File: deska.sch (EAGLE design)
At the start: 15 parts, among them T1 TIP122, T2 TIP122, T3 TIP122, X2 NAPAJENI

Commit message: deska
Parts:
- removed X2: NAPAJENI, con-wago-508:W237-05P
- added LISTA: (no value), con-wago-500:W237-6
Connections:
- net +12V: now also LISTA-4.KL, LISTA-5.KL; no longer X2-4.KL
- net GND: now also LISTA-6.KL; no longer X2-1.KL
- net N$1: now also LISTA-3.KL; no longer X2-5.KL
- net N$2: now also LISTA-2.KL; no longer X2-3.KL
- net N$3: now also LISTA-1.KL; no longer X2-2.KL
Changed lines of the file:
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@@
 <grid distance="0.1" unitdist="inch" unit="inch" style="lines" multiple="1" display="no" altdistance="0.01" altunitdist="inch" altunit="inch"/>
 <layers>
-<layer number="1" name="Top" color="4" fill="1" visible="no" active="no"/>
-<layer number="16" name="Bottom" color="1" fill="1" visible="no" active="no"/>
-<layer number="17" name="Pads" color="2" fill="1" visible="no" active="no"/>
-<layer number="18" name="Vias" color="2" fill="1" visible="no" active="no"/>
-<layer number="19" name="Unrouted" color="6" fill="1" visible="no" active="no"/>
-<layer number="20" name="Dimension" color="15" fill="1" visible="no" active="no"/>
-<layer number="21" name="tPlace" color="7" fill="1" visible="no" active="no"/>
-<layer number="22" name="bPlace" color="7" fill="1" visible="no" active="no"/>
-<layer number="23" name="tOrigins" color="15" fill="1" visible="no" active="no"/>
-<layer number="24" name="bOrigins" color="15" fill="1" visible="no" active="no"/>
-<layer number="25" name="tNames" color="7" fill="1" visible="no" active="no"/>
-<layer number="26" name="bNames" color="7" fill="1" visible="no" active="no"/>
-<layer number="27" name="tValues" color="7" fill="1" visible="no" active="no"/>
-<layer number="28" name="bValues" color="7" fill="1" visible="no" active="no"/>
+<layer number="1" name="Top" color="4" fill="1" visible="yes" active="no"/>
+<layer number="16" name="Bottom" color="1" fill="1" visible="yes" active="no"/>
+<layer number="17" name="Pads" color="2" fill="1" visible="yes" active="no"/>
+<layer number="18" name="Vias" color="2" fill="1" visible="yes" active="no"/>
+<layer number="19" name="Unrouted" color="6" fill="1" visible="yes" active="no"/>
+<layer number="20" name="Dimension" color="15" fill="1" visible="yes" active="no"/>
+<layer number="21" name="tPlace" color="7" fill="1" visible="yes" active="no"/>
+<layer number="22" name="bPlace" color="7" fill="1" visible="yes" active="no"/>
+<layer number="23" name="tOrigins" color="15" fill="1" visible="yes" active="no"/>
+<layer number="24" name="bOrigins" color="15" fill="1" visible="yes" active="no"/>
+<layer number="25" name="tNames" color="7" fill="1" visible="yes" active="no"/>
+<layer number="26" name="bNames" color="7" fill="1" visible="yes" active="no"/>
+<layer number="27" name="tValues" color="7" fill="1" visible="yes" active="no"/>
+<layer number="28" name="bValues" color="7" fill="1" visible="yes" active="no"/>
 <layer number="29" name="tStop" color="7" fill="3" visible="no" active="no"/>
 <layer number="30" name="bStop" color="7" fill="6" visible="no" active="no"/>
@@
 <layer number="35" name="tGlue" color="7" fill="4" visible="no" active="no"/>
 <layer number="36" name="bGlue" color="7" fill="5" visible="no" active="no"/>
-<layer number="37" name="tTest" color="7" fill="1" visible="no" active="no"/>
-<layer number="38" name="bTest" color="7" fill="1" visible="no" active="no"/>
+<layer number="37" name="tTest" color="7" fill="1" visible="yes" active="no"/>
+<layer number="38" name="bTest" color="7" fill="1" visible="yes" active="no"/>
 <layer number="39" name="tKeepout" color="4" fill="11" visible="no" active="no"/>
 <layer number="40" name="bKeepout" color="1" fill="11" visible="no" active="no"/>
@@
 <layer number="44" name="Drills" color="7" fill="1" visible="no" active="no"/>
 <layer number="45" name="Holes" color="7" fill="1" visible="no" active="no"/>
-<layer number="46" name="Milling" color="3" fill="1" visible="no" active="no"/>
-<layer number="47" name="Measures" color="7" fill="1" visible="no" active="no"/>
-<layer number="48" name="Document" color="7" fill="1" visible="no" active="no"/>
-<layer number="49" name="Reference" color="7" fill="1" visible="no" active="no"/>
-<layer number="51" name="tDocu" color="7" fill="1" visible="no" active="no"/>
-<layer number="52" name="bDocu" color="7" fill="1" visible="no" active="no"/>
+<layer number="46" name="Milling" color="3" fill="1" visible="yes" active="no"/>
+<layer number="47" name="Measures" color="7" fill="1" visible="yes" active="no"/>
+<layer number="48" name="Document" color="7" fill="1" visible="yes" active="no"/>
+<layer number="49" name="Reference" color="7" fill="1" visible="yes" active="no"/>
+<layer number="51" name="tDocu" color="7" fill="1" visible="yes" active="no"/>
+<layer number="52" name="bDocu" color="7" fill="1" visible="yes" active="no"/>
 <layer number="90" name="Modules" color="5" fill="1" visible="yes" active="yes"/>
 <layer number="91" name="Nets" color="2" fill="1" visible="yes" active="yes"/>
@@
 <part name="R3" library="rcl" deviceset="R-EU_" device="0207/10" value="1k"/>
 <part name="GND6" library="supply1" deviceset="GND" device=""/>
-<part name="X2" library="con-wago-508" deviceset="W237-05P" device="" value="NAPAJENI"/>
 <part name="GND4" library="supply1" deviceset="GND" device=""/>
 <part name="SV1" library="con-lstb" deviceset="MA04-2" device="" value="ESP8266"/>
@@
 <part name="GND5" library="supply1" deviceset="GND" device=""/>
 <part name="TX" library="con-amp-quick" library_urn="urn:adsk.eagle:library:125" deviceset="M02" device="" package3d_urn="urn:adsk.eagle:package:5956/1" value="TX"/>
+<part name="LISTA" library="con-wago-500" library_urn="urn:adsk.eagle:library:195" deviceset="W237-6" device="" package3d_urn="urn:adsk.eagle:package:10696/1"/>
 </parts>
 <sheets>
@@
 <instance part="R3" gate="G$1" x="73.66" y="66.04"/>
 <instance part="GND6" gate="1" x="-22.86" y="40.64"/>
-<instance part="X2" gate="-1" x="53.34" y="96.52" rot="R270"/>
-<instance part="X2" gate="-2" x="48.26" y="96.52" rot="R270"/>
-<instance part="X2" gate="-3" x="43.18" y="96.52" rot="R270"/>
-<instance part="X2" gate="-4" x="38.1" y="96.52" rot="R270"/>
-<instance part="X2" gate="-5" x="33.02" y="96.52" rot="R270"/>
-<instance part="GND4" gate="1" x="53.34" y="88.9"/>
+<instance part="GND4" gate="1" x="33.02" y="91.44"/>
 <instance part="SV1" gate="G$1" x="0" y="48.26"/>
 <instance part="R4" gate="G$1" x="-12.7" y="66.04"/>
@@
 <instance part="GND5" gate="1" x="22.86" y="86.36"/>
 <instance part="TX" gate="G$1" x="2.54" y="20.32" rot="R90"/>
+<instance part="LISTA" gate="-1" x="63.5" y="99.06" rot="R270"/>
+<instance part="LISTA" gate="-2" x="58.42" y="99.06" rot="R270"/>
+<instance part="LISTA" gate="-3" x="53.34" y="99.06" rot="R270"/>
+<instance part="LISTA" gate="-4" x="48.26" y="99.06" rot="R270"/>
+<instance part="LISTA" gate="-5" x="38.1" y="101.6" rot="R270"/>
+<instance part="LISTA" gate="-6" x="33.02" y="101.6" rot="R270"/>
 </instances>
 <busses>
@@
 </segment>
 <segment>
-<pinref part="X2" gate="-1" pin="KL"/>
-<pinref part="GND4" gate="1" pin="GND"/>
-</segment>
-<segment>
 <pinref part="RESET" gate="1" pin="S"/>
 <pinref part="RESET" gate="2" pin="S"/>
@@
 <wire x1="22.86" y1="93.98" x2="22.86" y2="88.9" width="0.1524" layer="91"/>
 </segment>
+<segment>
+<pinref part="LISTA" gate="-6" pin="KL"/>
+<pinref part="GND4" gate="1" pin="GND"/>
+<wire x1="33.02" y1="93.98" x2="33.02" y2="96.52" width="0.1524" layer="91"/>
+</segment>
 </net>
 <net name="N$1" class="0">
@@
 <pinref part="T1" gate="G$1" pin="C"/>
 <wire x1="22.86" y1="68.58" x2="33.02" y2="68.58" width="0.1524" layer="91"/>
-<pinref part="X2" gate="-5" pin="KL"/>
-<wire x1="33.02" y1="91.44" x2="33.02" y2="68.58" width="0.1524" layer="91"/>
+<pinref part="LISTA" gate="-3" pin="KL"/>
+<wire x1="53.34" y1="93.98" x2="53.34" y2="86.36" width="0.1524" layer="91"/>
+<wire x1="53.34" y1="86.36" x2="53.34" y2="81.28" width="0.1524" layer="91"/>
+<wire x1="53.34" y1="81.28" x2="45.72" y2="81.28" width="0.1524" layer="91"/>
+<wire x1="45.72" y1="81.28" x2="33.02" y2="81.28" width="0.1524" layer="91"/>
+<wire x1="33.02" y1="81.28" x2="33.02" y2="68.58" width="0.1524" layer="91"/>
 </segment>
 </net>
 <net name="N$2" class="0">
 <segment>
-<wire x1="43.18" y1="91.44" x2="43.18" y2="76.2" width="0.1524" layer="91"/>
 <pinref part="T2" gate="G$1" pin="C"/>
-<wire x1="43.18" y1="76.2" x2="58.42" y2="76.2" width="0.1524" layer="91"/>
 <wire x1="58.42" y1="76.2" x2="58.42" y2="68.58" width="0.1524" layer="91"/>
-<pinref part="X2" gate="-3" pin="KL"/>
+<pinref part="LISTA" gate="-2" pin="KL"/>
+<wire x1="58.42" y1="93.98" x2="58.42" y2="76.2" width="0.1524" layer="91"/>
 </segment>
 </net>
@@
 <segment>
 <pinref part="T3" gate="G$1" pin="C"/>
-<wire x1="48.26" y1="91.44" x2="48.26" y2="83.82" width="0.1524" layer="91"/>
-<wire x1="48.26" y1="83.82" x2="86.36" y2="83.82" width="0.1524" layer="91"/>
-<wire x1="86.36" y1="83.82" x2="86.36" y2="68.58" width="0.1524" layer="91"/>
-<pinref part="X2" gate="-2" pin="KL"/>
+<pinref part="LISTA" gate="-1" pin="KL"/>
+<wire x1="86.36" y1="81.28" x2="86.36" y2="68.58" width="0.1524" layer="91"/>
+<wire x1="63.5" y1="93.98" x2="63.5" y2="81.28" width="0.1524" layer="91"/>
+<wire x1="63.5" y1="81.28" x2="86.36" y2="81.28" width="0.1524" layer="91"/>
 </segment>
 </net>
@@
 <net name="+12V" class="0">
 <segment>
-<pinref part="X2" gate="-4" pin="KL"/>
 <pinref part="P+1" gate="1" pin="+12V"/>
-<wire x1="38.1" y1="88.9" x2="38.1" y2="91.44" width="0.1524" layer="91"/>
 <pinref part="SL1" gate="G$1" pin="3"/>
 <wire x1="17.78" y1="96.52" x2="27.94" y2="96.52" width="0.1524" layer="91"/>
 <wire x1="27.94" y1="96.52" x2="27.94" y2="88.9" width="0.1524" layer="91"/>
 <wire x1="27.94" y1="88.9" x2="38.1" y2="88.9" width="0.1524" layer="91"/>
+<pinref part="LISTA" gate="-5" pin="KL"/>
+<wire x1="38.1" y1="96.52" x2="38.1" y2="88.9" width="0.1524" layer="91"/>
 <junction x="38.1" y="88.9"/>
-</segment>
-</net>
+<wire x1="38.1" y1="88.9" x2="48.26" y2="88.9" width="0.1524" layer="91"/>
+<pinref part="LISTA" gate="-4" pin="KL"/>
+<wire x1="48.26" y1="88.9" x2="48.26" y2="93.98" width="0.1524" layer="91"/>
+</segment>
+</net>

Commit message: deska
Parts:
- removed TX: TX, con-amp-quick:M02
- added SERIAL: (no value), con-amp-quick:M03
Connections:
- net GND: now also SERIAL.1; no longer TX.2
- net N$7: now also SERIAL.3
- net N$9: now also SERIAL.2; no longer TX.1
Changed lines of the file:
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@@
 <grid distance="0.1" unitdist="inch" unit="inch" style="lines" multiple="1" display="no" altdistance="0.01" altunitdist="inch" altunit="inch"/>
 <layers>
-<layer number="1" name="Top" color="4" fill="1" visible="yes" active="no"/>
-<layer number="16" name="Bottom" color="1" fill="1" visible="yes" active="no"/>
-<layer number="17" name="Pads" color="2" fill="1" visible="yes" active="no"/>
-<layer number="18" name="Vias" color="2" fill="1" visible="yes" active="no"/>
-<layer number="19" name="Unrouted" color="6" fill="1" visible="yes" active="no"/>
-<layer number="20" name="Dimension" color="15" fill="1" visible="yes" active="no"/>
-<layer number="21" name="tPlace" color="7" fill="1" visible="yes" active="no"/>
-<layer number="22" name="bPlace" color="7" fill="1" visible="yes" active="no"/>
-<layer number="23" name="tOrigins" color="15" fill="1" visible="yes" active="no"/>
-<layer number="24" name="bOrigins" color="15" fill="1" visible="yes" active="no"/>
-<layer number="25" name="tNames" color="7" fill="1" visible="yes" active="no"/>
-<layer number="26" name="bNames" color="7" fill="1" visible="yes" active="no"/>
-<layer number="27" name="tValues" color="7" fill="1" visible="yes" active="no"/>
-<layer number="28" name="bValues" color="7" fill="1" visible="yes" active="no"/>
+<layer number="1" name="Top" color="4" fill="1" visible="no" active="no"/>
+<layer number="16" name="Bottom" color="1" fill="1" visible="no" active="no"/>
+<layer number="17" name="Pads" color="2" fill="1" visible="no" active="no"/>
+<layer number="18" name="Vias" color="2" fill="1" visible="no" active="no"/>
+<layer number="19" name="Unrouted" color="6" fill="1" visible="no" active="no"/>
+<layer number="20" name="Dimension" color="15" fill="1" visible="no" active="no"/>
+<layer number="21" name="tPlace" color="7" fill="1" visible="no" active="no"/>
+<layer number="22" name="bPlace" color="7" fill="1" visible="no" active="no"/>
+<layer number="23" name="tOrigins" color="15" fill="1" visible="no" active="no"/>
+<layer number="24" name="bOrigins" color="15" fill="1" visible="no" active="no"/>
+<layer number="25" name="tNames" color="7" fill="1" visible="no" active="no"/>
+<layer number="26" name="bNames" color="7" fill="1" visible="no" active="no"/>
+<layer number="27" name="tValues" color="7" fill="1" visible="no" active="no"/>
+<layer number="28" name="bValues" color="7" fill="1" visible="no" active="no"/>
 <layer number="29" name="tStop" color="7" fill="3" visible="no" active="no"/>
 <layer number="30" name="bStop" color="7" fill="6" visible="no" active="no"/>
@@
 <layer number="35" name="tGlue" color="7" fill="4" visible="no" active="no"/>
 <layer number="36" name="bGlue" color="7" fill="5" visible="no" active="no"/>
-<layer number="37" name="tTest" color="7" fill="1" visible="yes" active="no"/>
-<layer number="38" name="bTest" color="7" fill="1" visible="yes" active="no"/>
+<layer number="37" name="tTest" color="7" fill="1" visible="no" active="no"/>
+<layer number="38" name="bTest" color="7" fill="1" visible="no" active="no"/>
 <layer number="39" name="tKeepout" color="4" fill="11" visible="no" active="no"/>
 <layer number="40" name="bKeepout" color="1" fill="11" visible="no" active="no"/>
@@
 <layer number="44" name="Drills" color="7" fill="1" visible="no" active="no"/>
 <layer number="45" name="Holes" color="7" fill="1" visible="no" active="no"/>
-<layer number="46" name="Milling" color="3" fill="1" visible="yes" active="no"/>
-<layer number="47" name="Measures" color="7" fill="1" visible="yes" active="no"/>
-<layer number="48" name="Document" color="7" fill="1" visible="yes" active="no"/>
-<layer number="49" name="Reference" color="7" fill="1" visible="yes" active="no"/>
-<layer number="51" name="tDocu" color="7" fill="1" visible="yes" active="no"/>
-<layer number="52" name="bDocu" color="7" fill="1" visible="yes" active="no"/>
+<layer number="46" name="Milling" color="3" fill="1" visible="no" active="no"/>
+<layer number="47" name="Measures" color="7" fill="1" visible="no" active="no"/>
+<layer number="48" name="Document" color="7" fill="1" visible="no" active="no"/>
+<layer number="49" name="Reference" color="7" fill="1" visible="no" active="no"/>
+<layer number="51" name="tDocu" color="7" fill="1" visible="no" active="no"/>
+<layer number="52" name="bDocu" color="7" fill="1" visible="no" active="no"/>
 <layer number="90" name="Modules" color="5" fill="1" visible="yes" active="yes"/>
 <layer number="91" name="Nets" color="2" fill="1" visible="yes" active="yes"/>
@@
 <part name="SL1" library="con-amp-quick" library_urn="urn:adsk.eagle:library:125" deviceset="M03" device="" package3d_urn="urn:adsk.eagle:package:5957/1" value="DCDC"/>
 <part name="GND5" library="supply1" deviceset="GND" device=""/>
-<part name="TX" library="con-amp-quick" library_urn="urn:adsk.eagle:library:125" deviceset="M02" device="" package3d_urn="urn:adsk.eagle:package:5956/1" value="TX"/>
 <part name="LISTA" library="con-wago-500" library_urn="urn:adsk.eagle:library:195" deviceset="W237-6" device="" package3d_urn="urn:adsk.eagle:package:10696/1"/>
+<part name="SERIAL" library="con-amp-quick" library_urn="urn:adsk.eagle:library:125" deviceset="M03" device="" package3d_urn="urn:adsk.eagle:package:5957/1"/>
 </parts>
 <sheets>
@@
 <instance part="SL1" gate="G$1" x="10.16" y="93.98"/>
 <instance part="GND5" gate="1" x="22.86" y="86.36"/>
-<instance part="TX" gate="G$1" x="2.54" y="20.32" rot="R90"/>
 <instance part="LISTA" gate="-1" x="63.5" y="99.06" rot="R270"/>
 <instance part="LISTA" gate="-2" x="58.42" y="99.06" rot="R270"/>
@@
 <instance part="LISTA" gate="-5" x="38.1" y="101.6" rot="R270"/>
 <instance part="LISTA" gate="-6" x="33.02" y="101.6" rot="R270"/>
+<instance part="SERIAL" gate="G$1" x="0" y="15.24" rot="R90"/>
 </instances>
 <busses>
@@
 <wire x1="-22.86" y1="43.18" x2="-7.62" y2="43.18" width="0.1524" layer="91"/>
 <pinref part="SV1" gate="G$1" pin="2"/>
-<pinref part="TX" gate="G$1" pin="2"/>
-<wire x1="0" y1="27.94" x2="-7.62" y2="27.94" width="0.1524" layer="91"/>
-<wire x1="-7.62" y1="27.94" x2="-7.62" y2="43.18" width="0.1524" layer="91"/>
+<wire x1="-7.62" y1="43.18" x2="-7.62" y2="25.4" width="0.1524" layer="91"/>
+<wire x1="-7.62" y1="25.4" x2="2.54" y2="25.4" width="0.1524" layer="91"/>
 <junction x="-7.62" y="43.18"/>
+<pinref part="SERIAL" gate="G$1" pin="1"/>
+<wire x1="2.54" y1="25.4" x2="2.54" y2="22.86" width="0.1524" layer="91"/>
 </segment>
 <segment>
@@
 <pinref part="R4" gate="G$1" pin="2"/>
 <junction x="-7.62" y="66.04"/>
+<wire x1="-7.62" y1="50.8" x2="-10.16" y2="50.8" width="0.1524" layer="91"/>
+<wire x1="-10.16" y1="50.8" x2="-10.16" y2="25.4" width="0.1524" layer="91"/>
+<junction x="-7.62" y="50.8"/>
+<pinref part="SERIAL" gate="G$1" pin="3"/>
+<wire x1="-10.16" y1="25.4" x2="-10.16" y2="22.86" width="0.1524" layer="91"/>
+<wire x1="-10.16" y1="22.86" x2="-2.54" y2="22.86" width="0.1524" layer="91"/>
 </segment>
 </net>
@@
 </segment>
 </net>
-<net name="N$9" class="0">
-<segment>
-<pinref part="SV1" gate="G$1" pin="1"/>
-<wire x1="7.62" y1="43.18" x2="7.62" y2="27.94" width="0.1524" layer="91"/>
-<pinref part="TX" gate="G$1" pin="1"/>
-<wire x1="7.62" y1="27.94" x2="2.54" y2="27.94" width="0.1524" layer="91"/>
-</segment>
-</net>
 <net name="+12V" class="0">
 <segment>
@@
 </segment>
 </net>
+<net name="N$9" class="0">
+<segment>
+<pinref part="SV1" gate="G$1" pin="1"/>
+<wire x1="7.62" y1="43.18" x2="7.62" y2="38.1" width="0.1524" layer="91"/>
+<wire x1="7.62" y1="38.1" x2="0" y2="38.1" width="0.1524" layer="91"/>
+<pinref part="SERIAL" gate="G$1" pin="2"/>
+<wire x1="0" y1="38.1" x2="0" y2="22.86" width="0.1524" layer="91"/>
+</segment>
+</net>

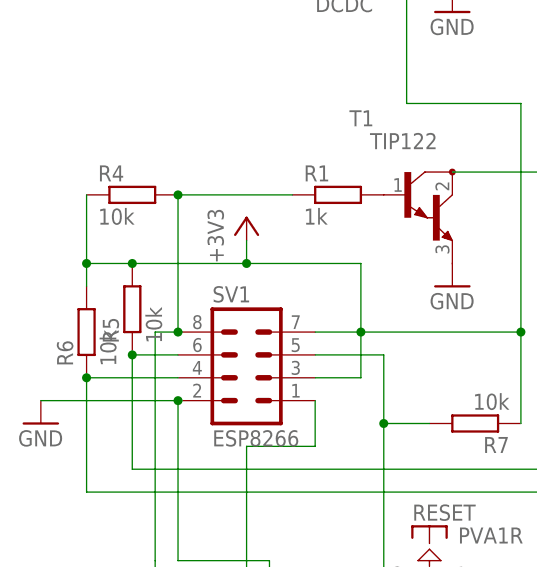
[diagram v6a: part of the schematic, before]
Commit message: zmena odporu
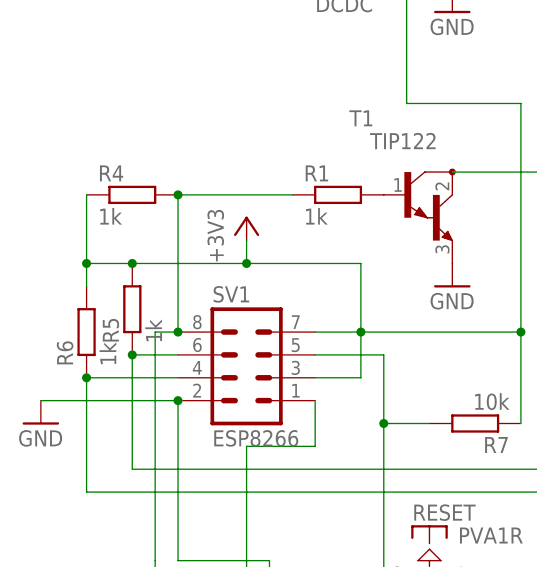
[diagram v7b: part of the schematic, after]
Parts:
- R4, R5, R6: value 10k -> 1k
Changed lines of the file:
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@@
 <part name="GND4" library="supply1" deviceset="GND" device=""/>
 <part name="SV1" library="con-lstb" deviceset="MA04-2" device="" value="ESP8266"/>
-<part name="R4" library="rcl" deviceset="R-EU_" device="0207/10" value="10k"/>
-<part name="R5" library="rcl" deviceset="R-EU_" device="0207/10" value="10k"/>
-<part name="R6" library="rcl" deviceset="R-EU_" device="0207/10" value="10k"/>
+<part name="R4" library="rcl" deviceset="R-EU_" device="0207/10" value="1k"/>
+<part name="R5" library="rcl" deviceset="R-EU_" device="0207/10" value="1k"/>
+<part name="R6" library="rcl" deviceset="R-EU_" device="0207/10" value="1k"/>
 <part name="R7" library="rcl" deviceset="R-EU_" device="0207/10" value="10k"/>
 <part name="RESET" library="switch-misc" library_urn="urn:adsk.eagle:library:376" deviceset="PVA1R" device="" package3d_urn="urn:adsk.eagle:package:27429/1"/>
